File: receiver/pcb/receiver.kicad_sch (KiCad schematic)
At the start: 24 parts, among them U1 RZ7886, U2 RZ7886, U3 XIAO ESP32C3

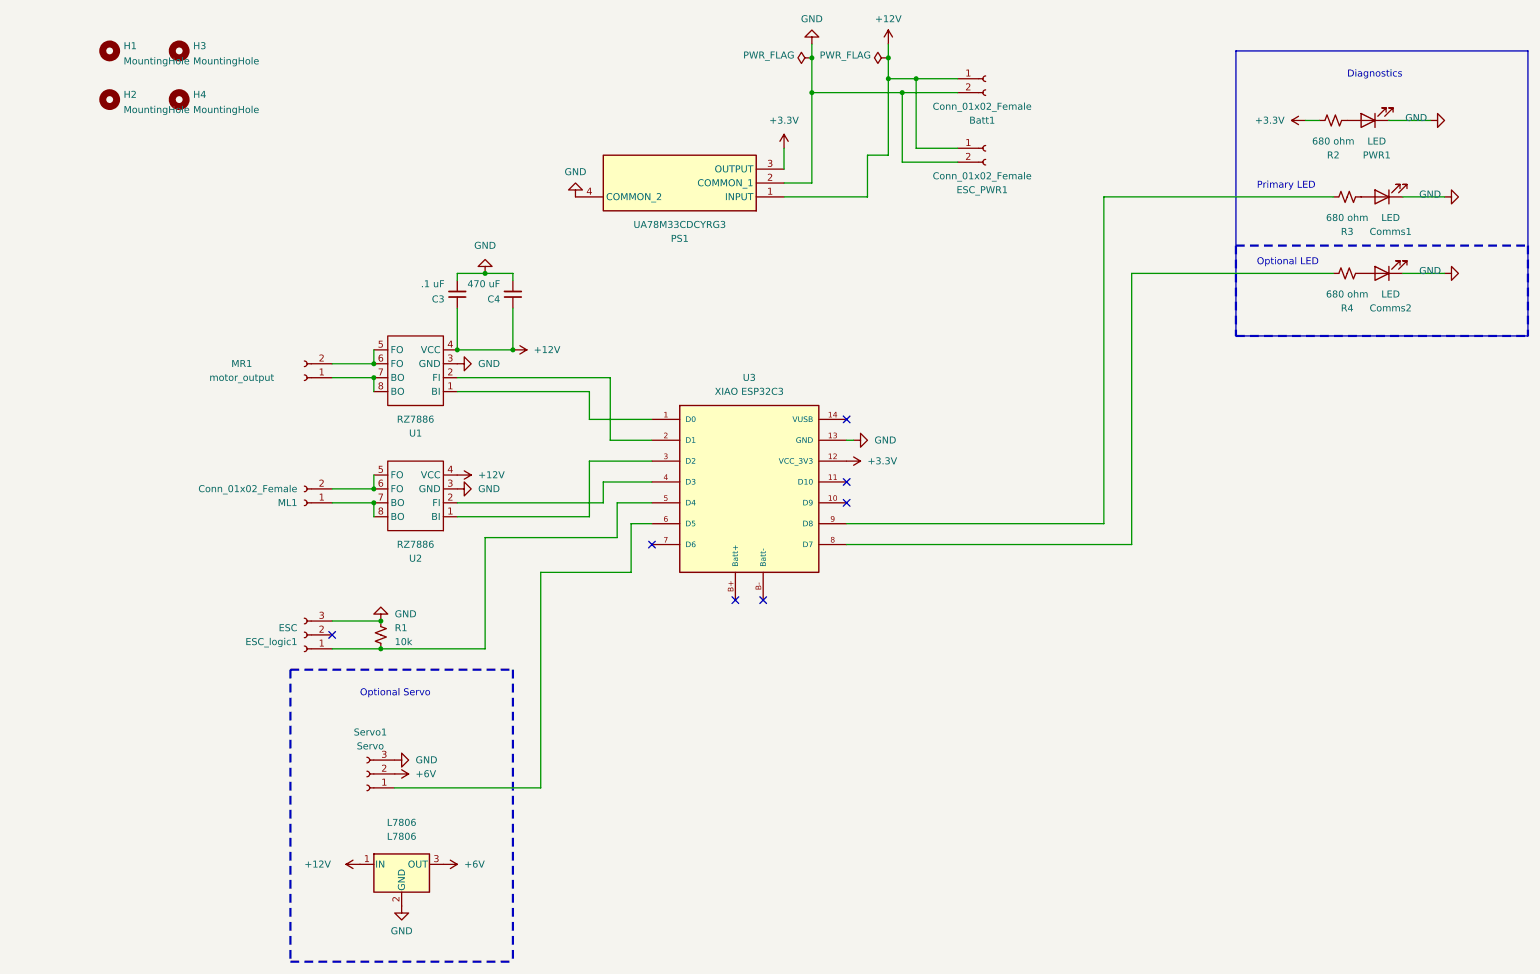
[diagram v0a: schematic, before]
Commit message: draft schematic with VNH7100BAS
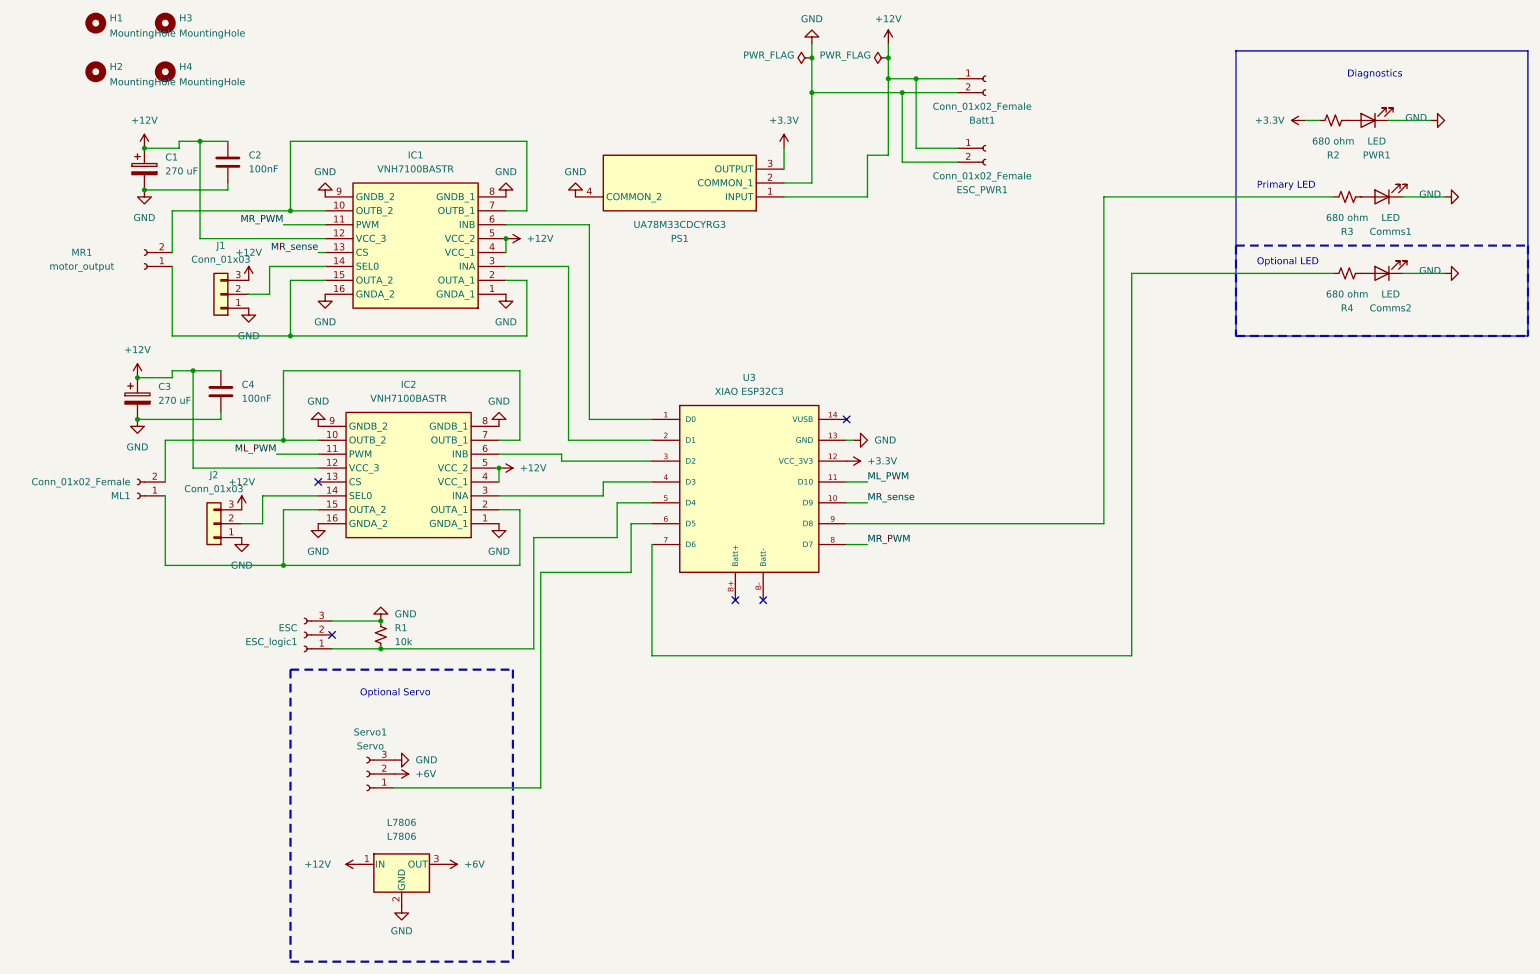
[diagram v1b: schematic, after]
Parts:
- removed C3: .1 uF, Capacitor_SMD:C_0805_2012Metric_Pad1.18x1.45mm_HandSolder, symbol Device:C_Small
- removed C4: 470 uF, Capacitor_THT:CP_Radial_D8.0mm_P3.80mm, symbol Device:C_Small
- removed U1, U2: RZ7886, Package_DIP:DIP-8_W7.62mm, symbol RZ7886:RZ7886
- added C1, C3: 270 uF, symbol Device:C_Polarized
- added C2, C4: 100nF, symbol Device:C
- added IC1, IC2: VNH7100BASTR, SOIC127P600X175-16N, symbol VNH7100BASTR:VNH7100BASTR
- added J1, J2: Conn_01x03, symbol Connector_Generic:Conn_01x03
- ML1: footprint Connector_PinSocket_2.54mm:PinSocket_1x02_P2.54mm_Vertical -> custom:DC_motor_output
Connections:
- net +12V: now also C1.1, C2.1, C3.1, C4.1, IC1.12 (VCC_3), IC1.4 (VCC_1), IC1.5 (VCC_2), IC2.12 (VCC_3), IC2.4 (VCC_1), IC2.5 (VCC_2), J1.3 (Pin_3), J2.3 (Pin_3)
- net GND: now also C1.2, C2.2, C3.2, C4.2, IC1.1 (GNDA_1), IC1.16 (GNDA_2), IC1.8 (GNDB_1), IC1.9 (GNDB_2), IC2.1 (GNDA_1), IC2.16 (GNDA_2), IC2.8 (GNDB_1), IC2.9 (GNDB_2), J1.1 (Pin_1), J2.1 (Pin_1)
- net at R4.1: now also U3.7 (D6); no longer U3.8 (D7)
- net at U3.1 (D0): now also IC1.6 (INB)
- net MR_sense: now reaches U3.10 (D9)
- net MR_sense: now also IC1.13 (CS)
- net ML_PWM: now reaches U3.11 (D10)
- net ML_PWM: now also IC2.11 (PWM)
- net at U3.2 (D1): now also IC1.3 (INA)
- net at U3.3 (D2): now also IC2.6 (INB)
- net at U3.4 (D3): now also IC2.3 (INA)
- net at ML1.1 (Pin_1): now also IC2.15 (OUTA_2), IC2.2 (OUTA_1)
- net at ML1.2 (Pin_2): now also IC2.10 (OUTB_2), IC2.7 (OUTB_1)
- net at MR1.2 (Pin_2): now also IC1.10 (OUTB_2), IC1.7 (OUTB_1)
- net at MR1.1 (Pin_1): now also IC1.15 (OUTA_2), IC1.2 (OUTA_1)
- new net: IC2.14 (SEL0), J2.2 (Pin_2)
- new net: IC1.14 (SEL0), J1.2 (Pin_2)
- new net MR_PWM: IC1.11 (PWM), U3.8 (D7)
- no-connect marks 7 -> 5
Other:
- moved on the sheet: H1, H2, H3, H4, ML1, MR1

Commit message: V8 as ordered from jlcpcb. Order #: Y34-2569843A
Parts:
- removed C3: 270 uF, symbol Device:C_Polarized
- removed C4: 100nF, symbol Device:C
- removed J1, J2: Conn_01x03, symbol Connector_Generic:Conn_01x03
- removed L7806: L7806, Package_TO_SOT_SMD:TO-263-2_TabPin1, symbol Regulator_Linear:L7806
- added IC1: L7806CD2T-TR, TO254P1542X460-3N, symbol L7806CD2T-TR:L7806CD2T-TR
- added ML_selector1: ML_selector, Connector_PinHeader_2.54mm:PinHeader_1x03_P2.54mm_Vertical, symbol Connector:Conn_01x03_Female
- added MR_selector1: MR_selector, Connector_PinHeader_2.54mm:PinHeader_1x03_P2.54mm_Vertical, symbol Connector:Conn_01x03_Female
- C1: footprint (none) -> Capacitor_THT:CP_Radial_D8.0mm_P3.80mm
- C2: footprint (none) -> Capacitor_SMD:C_0805_2012Metric_Pad1.18x1.45mm_HandSolder
- ESC_logic1, Servo1: footprint Connector_PinSocket_2.54mm:PinSocket_1x03_P2.54mm_Vertical -> Connector_PinHeader_2.54mm:PinHeader_1x03_P2.54mm_Vertical
- renumbered IC2 to ML2, IC1 to MR2, U3 to U1
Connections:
- net +12V: now also IC1.1 (INPUT), ML_selector1.3 (Pin_3), MR_selector1.3 (Pin_3)
- net +6V: now also IC1.3 (OUTPUT)
- net GND: now also IC1.4 (GND_(THERMALPAD)), ML_selector1.1 (Pin_1), MR_selector1.1 (Pin_1)
- net at ML2.14 (SEL0): now also ML_selector1.2 (Pin_2)
- net at MR2.14 (SEL0): now also MR_selector1.2 (Pin_2)

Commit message: V9 ready to order
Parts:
- removed ML_selector1: ML_selector, Connector_PinHeader_2.54mm:PinHeader_1x03_P2.54mm_Vertical, symbol Connector:Conn_01x03_Female
- removed MR_selector1: MR_selector, Connector_PinHeader_2.54mm:PinHeader_1x03_P2.54mm_Vertical, symbol Connector:Conn_01x03_Female
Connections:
- no-connect marks 5 -> 7
